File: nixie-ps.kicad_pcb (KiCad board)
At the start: 2 copper layers, 46 x 23 mm, 19 parts, among them J1 Conn_01x04_Male, J2 Conn_01x04_Male, Q1 IRFH7185TRPBF, T1 EFD15_2WI, U1 LM3488MM

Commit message: Make project fully portable
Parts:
- R5: value 0 -> 0.02
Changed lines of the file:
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@@
     (uvia_drill 0.1)
+  )
+  (module lib_fp:PQFN_5X6MM (layer B.Cu)
+    (at 108.6612 114.2492)
+    (fp_text reference Q1 (at 4.1148 0.3048 180) (layer B.SilkS)
+      (effects (font (size 0.6 0.6) (thickness 0.15)) (justify mirror))
+    )
+    (fp_text value IRFH7185TRPBF (at 0.5 -5.5) (layer B.Fab)
+      (effects (font (size 1 1) (thickness 0.15)) (justify mirror))
+    )
+    (fp_line (start -3.5 -4.2) (end 3.5 -4.2) (layer B.CrtYd) (width 0.05))
+    (fp_line (start -3.5 4.2) (end -3.5 -4.2) (layer B.CrtYd) (width 0.05))
+    (fp_line (start 3.5 4.2) (end -3.5 4.2) (layer B.CrtYd) (width 0.05))
+    (fp_line (start 3.5 -4.2) (end 3.5 4.2) (layer B.CrtYd) (width 0.05))
+    (fp_poly (pts (xy -2.1 -1.7) (xy -2 -1.6) (xy -1.9 -1.6) (xy -1.7 -1.7)
+      (xy -1.7 -1.9) (xy -1.9 -2) (xy -2.1 -1.9)) (layer B.Fab) (width 0.15))
+    (fp_circle (center -1.9 -1.8) (end -1.7 -1.6) (layer B.Fab) (width 0.15))
+    (fp_line (start 2.5 -3) (end -2.5 -3) (layer B.Fab) (width 0.15))
+    (fp_line (start 2.5 3) (end 2.5 -3) (layer B.Fab) (width 0.15))
+    (fp_line (start -2.5 3) (end 2.5 3) (layer B.Fab) (width 0.15))
+    (fp_line (start -2.5 -3) (end -2.5 3) (layer B.Fab) (width 0.15))
+    (fp_poly (pts (xy -2.1 -1.8) (xy -2 -1.6) (xy -1.7 -1.7) (xy -1.8 -2)
+      (xy -2 -2)) (layer B.SilkS) (width 0.15))
+    (fp_circle (center -1.9 -1.8) (end -1.7 -1.7) (layer B.SilkS) (width 0.15))
+    (fp_line (start -2.576 -3.076) (end -2.576 3.076) (layer B.SilkS) (width 0.15))
+    (fp_line (start 2.576 -3.076) (end 2.576 3.076) (layer B.SilkS) (width 0.15))
+    (pad 8 smd rect (at -1.905 3) (size 0.6 1.35) (layers B.Cu B.Paste B.Mask)
+      (net 5 "Net-(D2-Pad1)"))
+    (pad 7 smd rect (at -0.635 3.048) (size 0.6 1.35) (layers B.Cu B.Paste B.Mask)
+      (net 5 "Net-(D2-Pad1)"))
+    (pad 6 smd rect (at 0.635 3.048) (size 0.6 1.35) (layers B.Cu B.Paste B.Mask)
+      (net 5 "Net-(D2-Pad1)"))
+    (pad 5 smd rect (at 1.905 3.095) (size 0.6 1.35) (layers B.Cu B.Paste B.Mask)
+      (net 5 "Net-(D2-Pad1)"))
+    (pad 5 smd rect (at 0 0.648) (size 4.41 3.545) (layers B.Cu B.Paste B.Mask)
+      (net 5 "Net-(D2-Pad1)"))
+    (pad 4 smd rect (at 1.905 -3.02) (size 0.6 1.35) (layers B.Cu B.Paste B.Mask)
+      (net 14 /DR))
+    (pad 3 smd rect (at 0.635 -3.02) (size 0.6 1.35) (layers B.Cu B.Paste B.Mask)
+      (net 13 /ISEN))
+    (pad 2 smd rect (at -0.635 -3.02) (size 0.6 1.35) (layers B.Cu B.Paste B.Mask)
+      (net 13 /ISEN))
+    (pad 1 smd rect (at -1.905 -3.02) (size 0.6 1.35) (layers B.Cu B.Paste B.Mask)
+      (net 13 /ISEN))
+    (model ${KIPRJMOD}/3d_models/PQFN_5X6MM.step
+      (at (xyz 0 0 0))
+      (scale (xyz 1 1 1))
+      (rotate (xyz -90 0 90))
+    )
   )
   (module lib_fp:CP_Elec_6.3x5.4 (layer F.Cu)
@@
       (effects (font (size 0.6 0.6) (thickness 0.15)) (justify mirror))
     )
-    (fp_text value 0 (at 0 -3.05 180) (layer B.Fab)
+    (fp_text value 0.02 (at 0 -3.05 180) (layer B.Fab)
       (effects (font (size 1 1) (thickness 0.15)) (justify mirror))
     )
@@
     )
   )
-  (module lib_fp:PQFN_5X6MM (layer B.Cu)
-    (at 108.6612 114.2492)
-    (fp_text reference Q1 (at 4.1148 0.3048 180) (layer B.SilkS)
-      (effects (font (size 0.6 0.6) (thickness 0.15)) (justify mirror))
-    )
-    (fp_text value IRFH7185TRPBF (at 0.5 -5.5) (layer B.Fab)
-      (effects (font (size 1 1) (thickness 0.15)) (justify mirror))
-    )
-    (fp_line (start 2.576 -3.076) (end 2.576 3.076) (layer B.SilkS) (width 0.15))
-    (fp_line (start -2.576 -3.076) (end -2.576 3.076) (layer B.SilkS) (width 0.15))
-    (fp_circle (center -1.9 -1.8) (end -1.7 -1.7) (layer B.SilkS) (width 0.15))
-    (fp_poly (pts (xy -2.1 -1.8) (xy -2 -1.6) (xy -1.7 -1.7) (xy -1.8 -2)
-      (xy -2 -2)) (layer B.SilkS) (width 0.15))
-    (fp_line (start -2.5 -3) (end -2.5 3) (layer B.Fab) (width 0.15))
-    (fp_line (start -2.5 3) (end 2.5 3) (layer B.Fab) (width 0.15))
-    (fp_line (start 2.5 3) (end 2.5 -3) (layer B.Fab) (width 0.15))
-    (fp_line (start 2.5 -3) (end -2.5 -3) (layer B.Fab) (width 0.15))
-    (fp_circle (center -1.9 -1.8) (end -1.7 -1.6) (layer B.Fab) (width 0.15))
-    (fp_poly (pts (xy -2.1 -1.7) (xy -2 -1.6) (xy -1.9 -1.6) (xy -1.7 -1.7)
-      (xy -1.7 -1.9) (xy -1.9 -2) (xy -2.1 -1.9)) (layer B.Fab) (width 0.15))
-    (fp_line (start 3.5 -4.2) (end 3.5 4.2) (layer B.CrtYd) (width 0.05))
-    (fp_line (start 3.5 4.2) (end -3.5 4.2) (layer B.CrtYd) (width 0.05))
-    (fp_line (start -3.5 4.2) (end -3.5 -4.2) (layer B.CrtYd) (width 0.05))
-    (fp_line (start -3.5 -4.2) (end 3.5 -4.2) (layer B.CrtYd) (width 0.05))
-    (pad 1 smd rect (at -1.905 -3.02) (size 0.6 1.35) (layers B.Cu B.Paste B.Mask)
-      (net 13 /ISEN))
-    (pad 2 smd rect (at -0.635 -3.02) (size 0.6 1.35) (layers B.Cu B.Paste B.Mask)
-      (net 13 /ISEN))
-    (pad 3 smd rect (at 0.635 -3.02) (size 0.6 1.35) (layers B.Cu B.Paste B.Mask)
-      (net 13 /ISEN))
-    (pad 4 smd rect (at 1.905 -3.02) (size 0.6 1.35) (layers B.Cu B.Paste B.Mask)
-      (net 14 /DR))
-    (pad 5 smd rect (at 0 0.648) (size 4.41 3.545) (layers B.Cu B.Paste B.Mask)
-      (net 5 "Net-(D2-Pad1)"))
-    (pad 5 smd rect (at 1.905 3.095) (size 0.6 1.35) (layers B.Cu B.Paste B.Mask)
-      (net 5 "Net-(D2-Pad1)"))
-    (pad 6 smd rect (at 0.635 3.048) (size 0.6 1.35) (layers B.Cu B.Paste B.Mask)
-      (net 5 "Net-(D2-Pad1)"))
-    (pad 7 smd rect (at -0.635 3.048) (size 0.6 1.35) (layers B.Cu B.Paste B.Mask)
-      (net 5 "Net-(D2-Pad1)"))
-    (pad 8 smd rect (at -1.905 3) (size 0.6 1.35) (layers B.Cu B.Paste B.Mask)
-      (net 5 "Net-(D2-Pad1)"))
-    (model ${KICAD_USER_3DMOD_DIR}/esynr3z_QFN.3dshapes/PQFN_5X6MM.step
-      (at (xyz 0 0 0))
-      (scale (xyz 1 1 1))
-      (rotate (xyz -90 0 90))
-    )
-  )

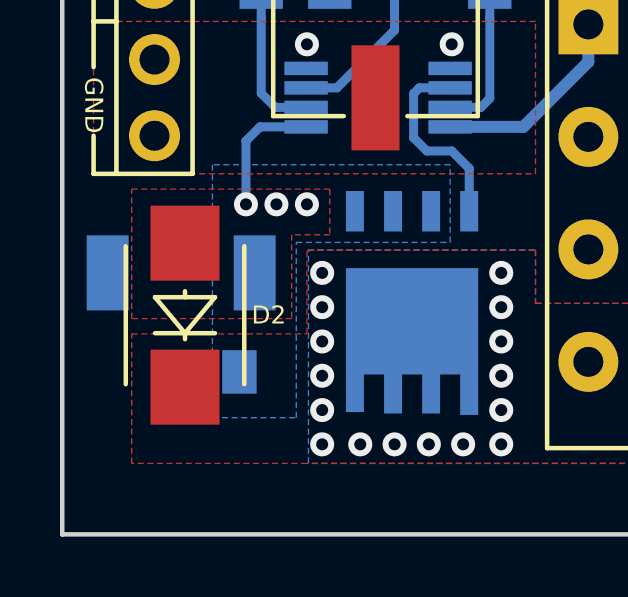
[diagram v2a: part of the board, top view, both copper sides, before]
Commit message: Update sch and pcb after latest simulation
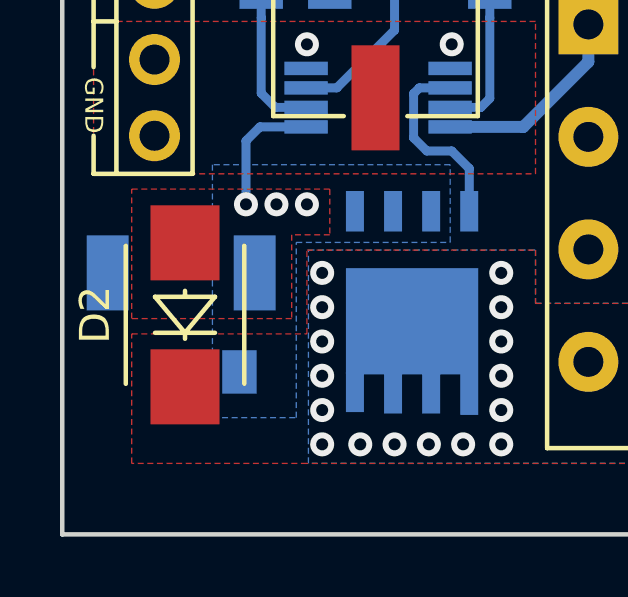
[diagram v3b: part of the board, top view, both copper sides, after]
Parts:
- D2: value SMBJ30CA -> SMBJ70CA
- R1: value 470k -> 1.2M
- R2: value 2.2k -> 7.5k
- R5: value 0.02 -> 0.01
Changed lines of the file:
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@@
       (at (xyz 0 0 0))
       (scale (xyz 1 1 1))
-      (rotate (xyz 0 0 0))
+      (rotate (xyz 0 0 180))
     )
   )
@@
     )
   )
-  (module lib_fp:SMB (layer F.Cu)
-    (at 101.092 114.694 90)
-    (descr "Diode SMB (DO-214AA)")
-    (tags "Diode SMB (DO-214AA)")
-    (attr smd)
-    (fp_text reference D2 (at 0 2.794 -180) (layer F.SilkS)
-      (effects (font (size 0.6 0.6) (thickness 0.15)))
-    )
-    (fp_text value SMBJ30CA (at -5.067 0.508 180) (layer F.Fab)
-      (effects (font (size 1 1) (thickness 0.15)))
-    )
-    (fp_text user %R (at 3.315 0 180) (layer F.Fab)
-      (effects (font (size 1 1) (thickness 0.15)))
-    )
-    (fp_line (start 2.3 2) (end -2.3 2) (layer F.Fab) (width 0.1))
-    (fp_line (start -2.3 2) (end -2.3 -2) (layer F.Fab) (width 0.1))
-    (fp_line (start 2.3 -2) (end 2.3 2) (layer F.Fab) (width 0.1))
-    (fp_line (start 2.3 -2) (end -2.3 -2) (layer F.Fab) (width 0.1))
-    (fp_line (start -3.8 -2.3) (end 3.8 -2.3) (layer F.CrtYd) (width 0.05))
-    (fp_line (start 3.8 -2.3) (end 3.8 2.3) (layer F.CrtYd) (width 0.05))
-    (fp_line (start 3.8 2.3) (end -3.8 2.3) (layer F.CrtYd) (width 0.05))
-    (fp_line (start -3.8 2.3) (end -3.8 -2.3) (layer F.CrtYd) (width 0.05))
-    (fp_line (start -0.64944 0.00102) (end -1.55114 0.00102) (layer F.Fab) (width 0.1))
-    (fp_line (start 0.50118 0.00102) (end 1.4994 0.00102) (layer F.Fab) (width 0.1))
-    (fp_line (start -0.64944 -0.79908) (end -0.64944 0.80112) (layer F.Fab) (width 0.1))
-    (fp_line (start 0.50118 0.75032) (end 0.50118 -0.79908) (layer F.Fab) (width 0.1))
-    (fp_line (start -0.64944 0.00102) (end 0.50118 0.75032) (layer F.Fab) (width 0.1))
-    (fp_line (start -0.64944 0.00102) (end 0.50118 -0.79908) (layer F.Fab) (width 0.1))
-    (fp_line (start -2.3 1.975) (end 2.3 1.975) (layer F.SilkS) (width 0.15))
-    (fp_line (start -2.3 -1.975) (end 2.3 -1.975) (layer F.SilkS) (width 0.15))
-    (fp_line (start -0.8 0) (end -0.6 0) (layer F.SilkS) (width 0.15))
-    (fp_line (start 0.8 0) (end 0.6 0) (layer F.SilkS) (width 0.15))
-    (fp_line (start 0.6 -1) (end 0.6 1) (layer F.SilkS) (width 0.15))
-    (fp_line (start 0.6 1) (end -0.6 0) (layer F.SilkS) (width 0.15))
-    (fp_line (start -0.6 0) (end 0.6 -1) (layer F.SilkS) (width 0.15))
-    (fp_line (start -0.6 -1) (end -0.6 1) (layer F.SilkS) (width 0.15))
-    (pad 1 smd rect (at -2.4 0 90) (size 2.5 2.3) (layers F.Cu F.Paste F.Mask)
-      (net 5 "Net-(D2-Pad1)"))
-    (pad 2 smd rect (at 2.4 0 90) (size 2.5 2.3) (layers F.Cu F.Paste F.Mask)
-      (net 13 /ISEN))
-    (model ${KISYS3DMOD}/Diode_SMD.3dshapes/D_SMB.wrl
-      (at (xyz 0 0 0))
-      (scale (xyz 1 1 1))
-      (rotate (xyz 0 0 0))
-    )
-  )
   (module lib_fp:0805 (layer F.Cu)
     (at 140.208 101.462 90)
@@
       (effects (font (size 0.6 0.6) (thickness 0.15)))
     )
-    (fp_text value 470k (at -2.805 0.254 180) (layer F.Fab)
+    (fp_text value 1.2M (at -2.805 0.254 180) (layer F.Fab)
       (effects (font (size 1 1) (thickness 0.15)))
     )
@@
       (effects (font (size 0.6 0.6) (thickness 0.15)))
     )
-    (fp_text value 2.2k (at 2.805 0.508) (layer F.Fab)
+    (fp_text value 7.5k (at 2.805 0.508) (layer F.Fab)
       (effects (font (size 1 1) (thickness 0.15)))
     )
@@
       (effects (font (size 0.6 0.6) (thickness 0.15)) (justify mirror))
     )
-    (fp_text value 0.02 (at 0.254 -2.032 180) (layer B.Fab)
+    (fp_text value 0.01 (at 0.254 -2.032 180) (layer B.Fab)
       (effects (font (size 1 1) (thickness 0.15)) (justify mirror))
     )
@@
       (at (xyz 0 0 0))
       (scale (xyz 1 1 1))
+      (rotate (xyz 0 0 0))
+    )
+  )
+  (module lib_fp:SMB (layer F.Cu)
+    (at 101.092 114.681 90)
+    (descr "Diode SMB (DO-214AA)")
+    (tags "Diode SMB (DO-214AA)")
+    (attr smd)
+    (fp_text reference D2 (at 0 -3 90) (layer F.SilkS)
+      (effects (font (size 1 1) (thickness 0.15)))
+    )
+    (fp_text value SMBJ70CA (at -5.08 0.508 180) (layer F.Fab)
+      (effects (font (size 1 1) (thickness 0.15)))
+    )
+    (fp_text user %R (at 0 -3 180) (layer F.Fab)
+      (effects (font (size 1 1) (thickness 0.15)))
+    )
+    (fp_line (start 2.3 2) (end -2.3 2) (layer F.Fab) (width 0.1))
+    (fp_line (start -2.3 2) (end -2.3 -2) (layer F.Fab) (width 0.1))
+    (fp_line (start 2.3 -2) (end 2.3 2) (layer F.Fab) (width 0.1))
+    (fp_line (start 2.3 -2) (end -2.3 -2) (layer F.Fab) (width 0.1))
+    (fp_line (start -3.8 -2.3) (end 3.8 -2.3) (layer F.CrtYd) (width 0.05))
+    (fp_line (start 3.8 -2.3) (end 3.8 2.3) (layer F.CrtYd) (width 0.05))
+    (fp_line (start 3.8 2.3) (end -3.8 2.3) (layer F.CrtYd) (width 0.05))
+    (fp_line (start -3.8 2.3) (end -3.8 -2.3) (layer F.CrtYd) (width 0.05))
+    (fp_line (start -0.64944 0.00102) (end -1.55114 0.00102) (layer F.Fab) (width 0.1))
+    (fp_line (start 0.50118 0.00102) (end 1.4994 0.00102) (layer F.Fab) (width 0.1))
+    (fp_line (start -0.64944 -0.79908) (end -0.64944 0.80112) (layer F.Fab) (width 0.1))
+    (fp_line (start 0.50118 0.75032) (end 0.50118 -0.79908) (layer F.Fab) (width 0.1))
+    (fp_line (start -0.64944 0.00102) (end 0.50118 0.75032) (layer F.Fab) (width 0.1))
+    (fp_line (start -0.64944 0.00102) (end 0.50118 -0.79908) (layer F.Fab) (width 0.1))
+    (fp_line (start -2.3 1.975) (end 2.3 1.975) (layer F.SilkS) (width 0.15))
+    (fp_line (start -2.3 -1.975) (end 2.3 -1.975) (layer F.SilkS) (width 0.15))
+    (fp_line (start -0.8 0) (end -0.6 0) (layer F.SilkS) (width 0.15))
+    (fp_line (start 0.8 0) (end 0.6 0) (layer F.SilkS) (width 0.15))
+    (fp_line (start 0.6 -1) (end 0.6 1) (layer F.SilkS) (width 0.15))
+    (fp_line (start 0.6 1) (end -0.6 0) (layer F.SilkS) (width 0.15))
+    (fp_line (start -0.6 0) (end 0.6 -1) (layer F.SilkS) (width 0.15))
+    (fp_line (start -0.6 -1) (end -0.6 1) (layer F.SilkS) (width 0.15))
+    (pad 1 smd rect (at -2.4 0 90) (size 2.5 2.3) (layers F.Cu F.Paste F.Mask)
+      (net 5 "Net-(D2-Pad1)"))
+    (pad 2 smd rect (at 2.4 0 90) (size 2.5 2.3) (layers F.Cu F.Paste F.Mask)
+      (net 13 /ISEN))
+    (model ${KIPRJMOD}/3d_models/D_SMB.wrl
+      (at (xyz 0 0 0))
+      (scale (xyz 1 1 1))

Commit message: Massive update after debuging and testing
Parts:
- R5: value 0.01 -> 0.033
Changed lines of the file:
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@@
   )
   (layers
-    (0 F.Cu signal)
+    (0 F.Cu signal hide)
     (31 B.Cu signal hide)
     (36 B.SilkS user hide)
@@
     (visible_elements FFFFFF7F)
     (pcbplotparams
-      (layerselection 0x20000_7fffffff)
+      (layerselection 0x10000_7ffffffe)
       (usegerberextensions true)
       (usegerberattributes false)
@@
       (subtractmaskfromsilk false)
       (outputformat 4)
-      (mirror false)
+      (mirror true)
       (drillshape 0)
       (scaleselection 1)
@@
       (effects (font (size 0.6 0.6) (thickness 0.15)) (justify mirror))
     )
-    (fp_text value 0.01 (at 0.254 -2.032 180) (layer B.Fab)
+    (fp_text value 0.033 (at 0.254 -2.032 180) (layer B.Fab)
       (effects (font (size 1 1) (thickness 0.15)) (justify mirror))
     )
